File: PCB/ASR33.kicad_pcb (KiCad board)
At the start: 2 copper layers, 45 x 27 mm, 42 parts, among them J1 USB-C, J2 DC, J3 Power, J4 RUN, J5 Tx, J6 Rx, Q1 NX7002AK, SW1 SW_Push, U1 ESP32-PICO-MINI-02, U2 FT231XQ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

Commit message: Production files
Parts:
- removed J1: USB-C, RevK:USC16-TR
- added J7: USB-C, RevK:USC16-TR, F.Cu at (124.3, 107.0)
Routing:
- net VBUS: track 18.0 -> 14.3 mm, vias 2 -> 0
- net GND: track 21.2 -> 22.5 mm
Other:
- board text added: "${CURRENT_DATE}"
- board text removed: "${DATE}"

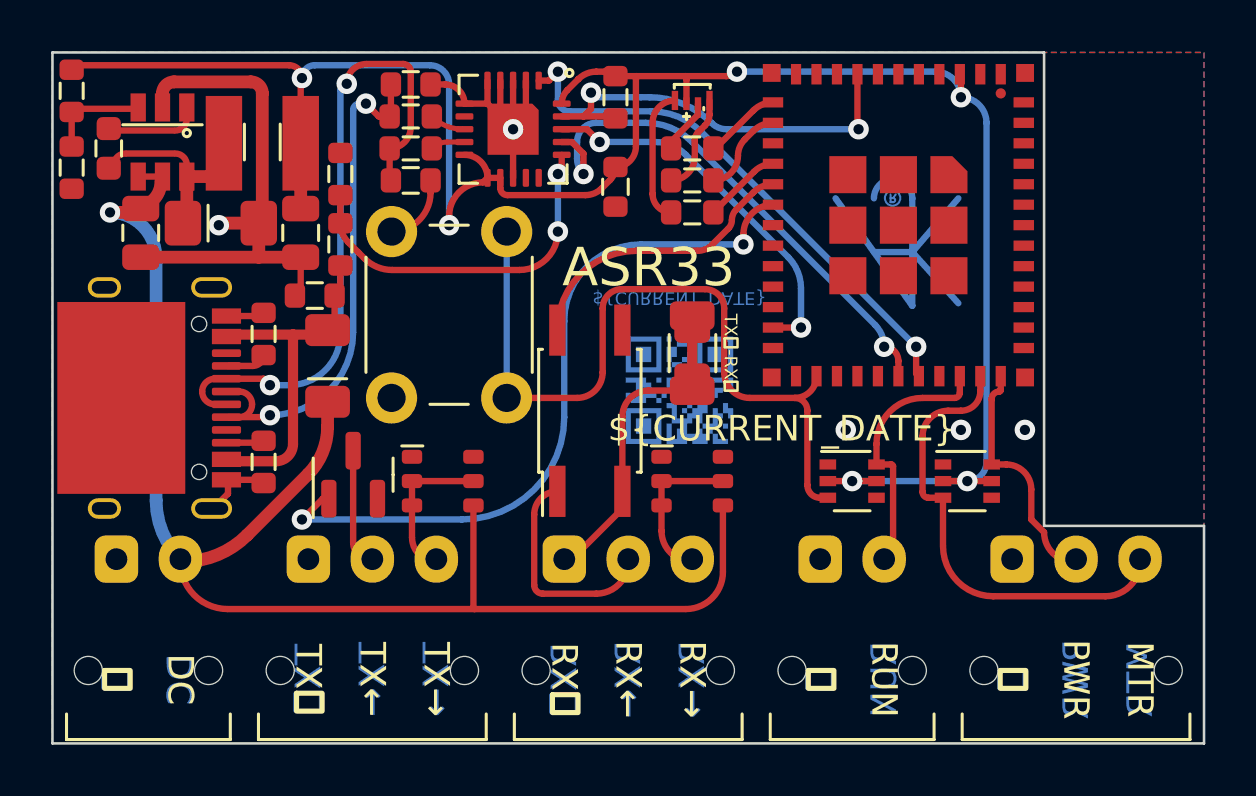
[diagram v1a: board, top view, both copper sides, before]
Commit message: Added programming header for when not using USB data
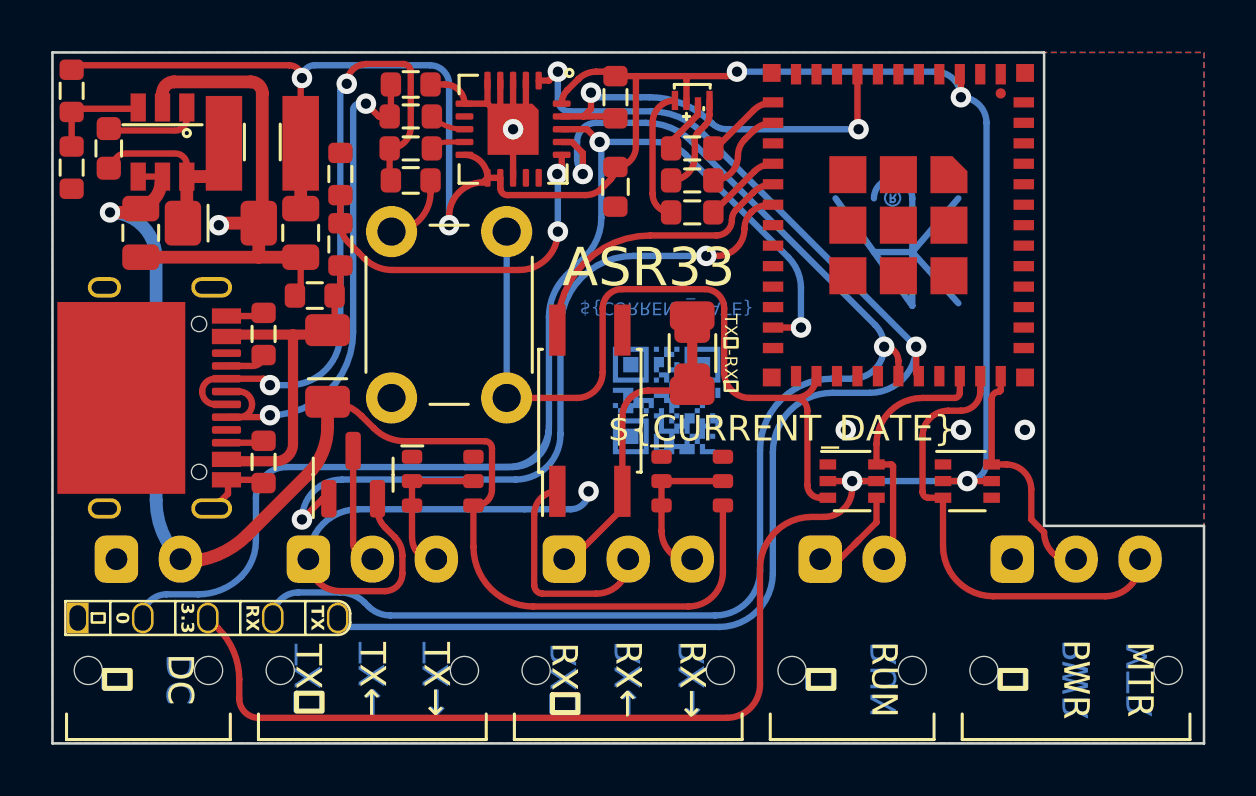
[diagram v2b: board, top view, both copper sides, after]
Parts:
- added J1: Shelly, RevK:Shelly, F.Cu at (126.1, 115.6)
- moved U7 0.64 mm to (144.0, 107.1)
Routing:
- net GPIO0: track 14.8 -> 51.3 mm
- net +3V3: track 81.0 -> 116.0 mm
- net I: track 20.7 -> 53.2 mm
- net O: track 21.1 -> 51.4 mm
- net GND: track 22.5 -> 46.8 mm, vias 5 -> 6
- net DC: track 55.9 -> 51.8 mm
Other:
- board text added: "USB 5V, or 4V-40V DC"
- board text removed: "4V-40V"

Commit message: Rework for 5 pin header instead of USB/USART
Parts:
- added C8: 1uF, RevK:C_0603, F.Cu at (146.7, 95.0)
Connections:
- U1 pad 12: R -> unconnected-(U1-IO32-Pad12)
- U1 pad 13: G -> unconnected-(U1-IO33-Pad13)
- U1 pad 15: B -> R
- U1 pad 16: RX20MA -> G
- U1 pad 17: TX20MA -> B
- U1 pad 18: unconnected-(U1-IO14-Pad18) -> RX20MA
- U1 pad 20: unconnected-(U1-IO13-Pad20) -> TX20MA
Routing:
- net EN: track 16.2 -> 18.0 mm, vias 2 -> 3
- net +3V3: track 116.0 -> 117.8 mm
- net G: track 3.50 -> 2.37 mm
- net TX20MA: track 28.3 -> 27.4 mm
- net RX20MA: track 11.4 -> 10.5 mm
- net B: track 3.07 -> 2.41 mm
- net R: track 3.03 -> 2.48 mm
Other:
- board text added: "(20mA loop)"
- board text added: "13"
- board text added: "14"
- board text added: "ASR33 Teletype Controller"
- board text added: "RGB: 25/26/27"
- board text removed: "26"
- board text removed: "27"
- board text removed: "ASR33 Controller"
- board text removed: "RGB: 32/33/25"
